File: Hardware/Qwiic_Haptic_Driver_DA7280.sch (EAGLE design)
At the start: 30 parts, among them J1 QWIIC_RIGHT_ANGLE, J2 QWIIC_RIGHT_ANGLE, M1 G1040003D_LRA_CASTELLATED, U1 HAPTIC_DRIVER_DA7280

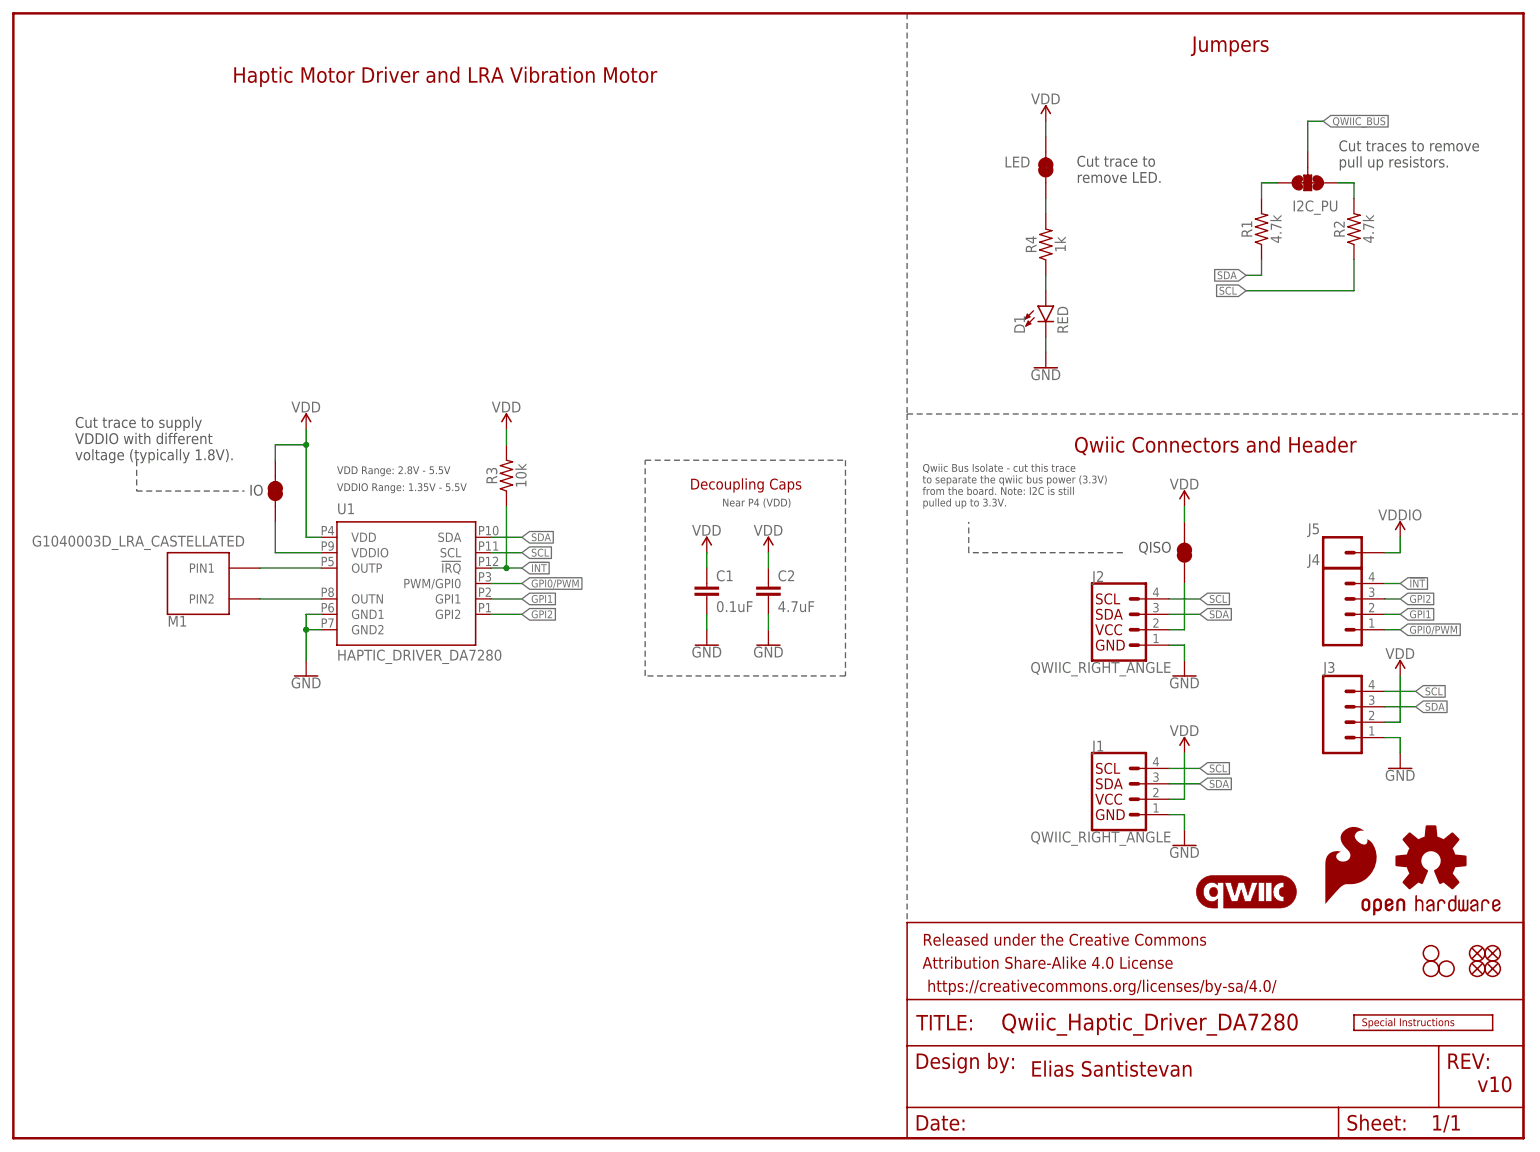
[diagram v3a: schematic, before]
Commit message: Adds second qwiic connecter to "qwiic bus" net so that the respective jumper can disconnect both
* Adds some power symbols
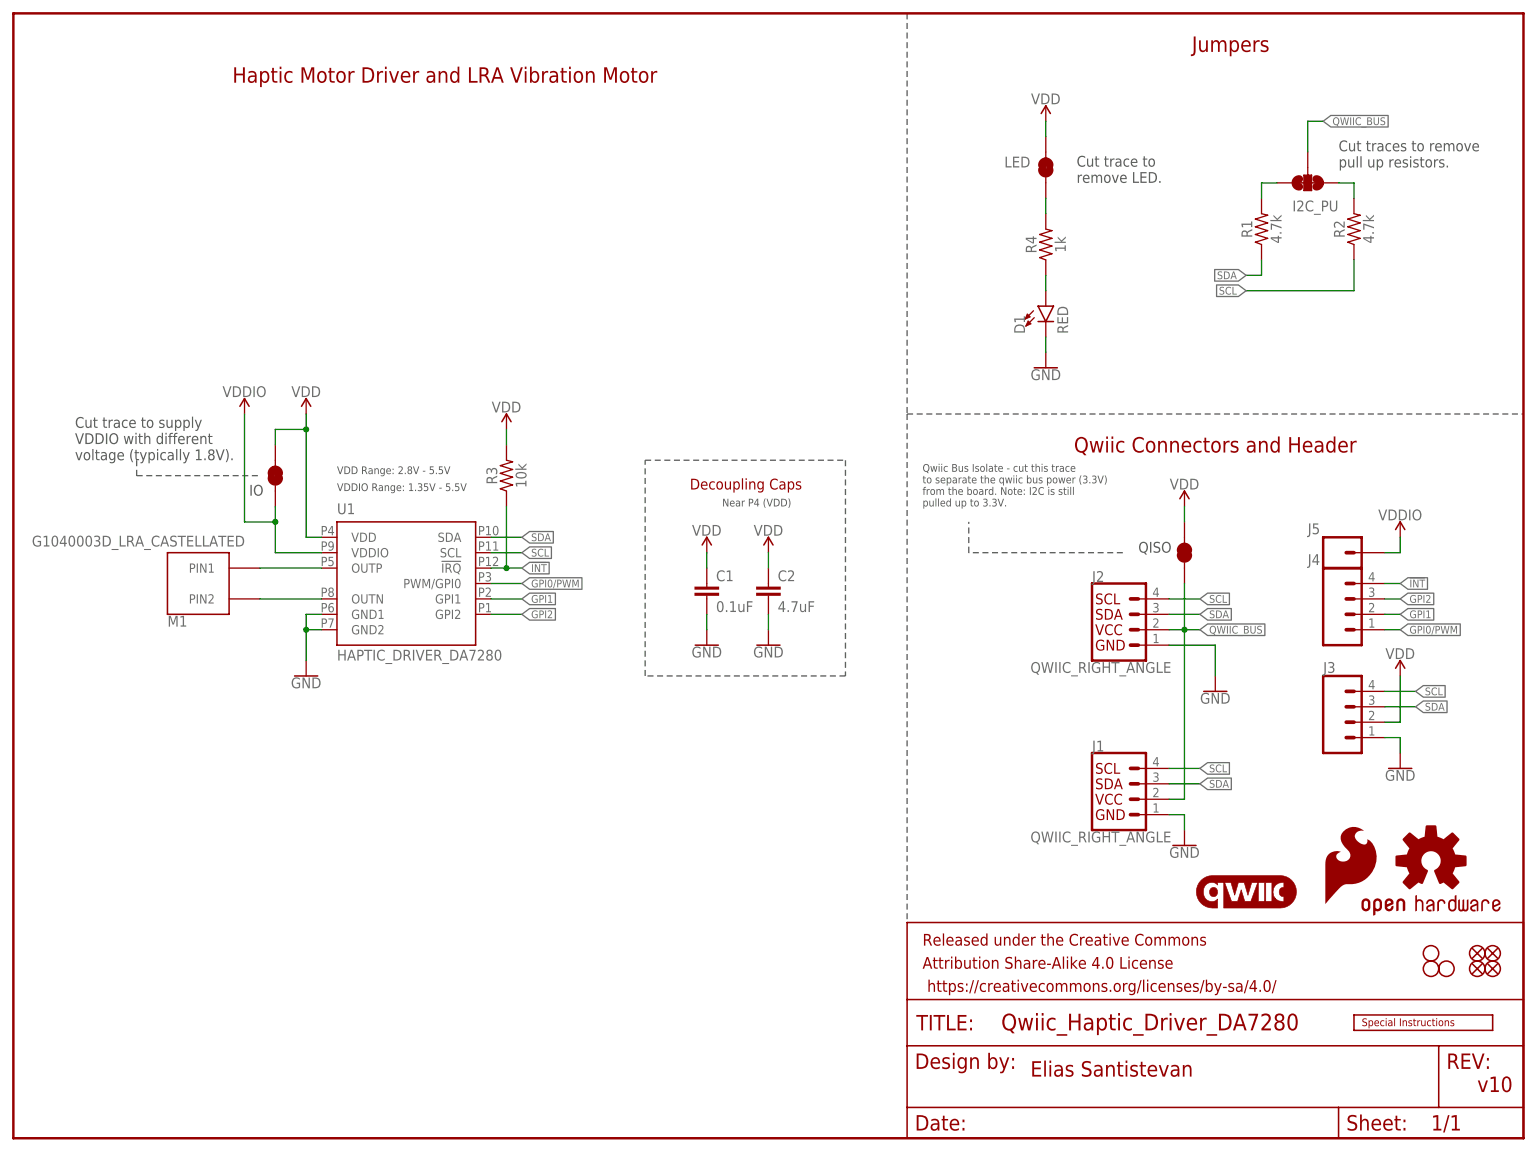
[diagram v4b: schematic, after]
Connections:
- net QWIIC_BUS: now also J1.2
- net VDD: no longer J1.2
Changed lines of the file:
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@@
 <part name="SUPPLY14" library="SparkFun-PowerSymbols" deviceset="VDD" device=""/>
 <part name="SUPPLY1" library="SparkFun-PowerSymbols" deviceset="VDD" device=""/>
-<part name="SUPPLY5" library="SparkFun-PowerSymbols" deviceset="VDD" device=""/>
 <part name="SUPPLY2" library="SparkFun-PowerSymbols" deviceset="VDD" device=""/>
 <part name="J5" library="SparkFun-Connectors" deviceset="CONN_01" device="PTH_NO_SILK_YES_STOP"/>
@@
 <part name="LOGO2" library="SparkFun-Aesthetics" deviceset="OSHW-LOGO" device="S"/>
 <part name="LOGO4" library="SparkFun-Aesthetics" deviceset="SFE_LOGO_FLAME" device=".1_INCH"/>
+<part name="SUPPLY4" library="SparkFun-PowerSymbols" deviceset="VDDIO" device=""/>
 </parts>
 <sheets>
@@
 voltage (typically 1.8V).
 </text>
-<wire x1="20.32" y1="111.76" x2="20.32" y2="106.68" width="0.2032" layer="97" style="dashdot"/>
-<wire x1="20.32" y1="106.68" x2="38.1" y2="106.68" width="0.2032" layer="97" style="dashdot"/>
+<wire x1="20.32" y1="111.76" x2="20.32" y2="109.22" width="0.2032" layer="97" style="dashdot"/>
+<wire x1="20.32" y1="109.22" x2="40.64" y2="109.22" width="0.2032" layer="97" style="dashdot"/>
 <text x="185.42" y="96.52" size="1.778" layer="97" font="vector">QISO</text>
 <text x="149.86" y="104.14" size="1.27" layer="97" font="vector">Qwiic Bus Isolate - cut this trace
@@
 <attribute name="VALUE" x="193.04" y="48.006" size="1.778" layer="96" font="vector" align="top-center"/>
 </instance>
-<instance part="GND3" gate="1" x="193.04" y="76.2" smashed="yes">
-<attribute name="VALUE" x="193.04" y="75.946" size="1.778" layer="96" font="vector" align="top-center"/>
+<instance part="GND3" gate="1" x="198.12" y="73.66" smashed="yes">
+<attribute name="VALUE" x="198.12" y="73.406" size="1.778" layer="96" font="vector" align="top-center"/>
 </instance>
 <instance part="GND4" gate="1" x="228.6" y="60.96" smashed="yes">
@@
 <attribute name="VALUE" x="124.46" y="81.026" size="1.778" layer="96" align="top-center"/>
 </instance>
-<instance part="JP2" gate="G$1" x="43.18" y="106.68" smashed="yes" rot="R90"/>
-<instance part="SUPPLY10" gate="VDD" x="48.26" y="116.84" smashed="yes">
-<attribute name="VALUE" x="48.26" y="119.634" size="1.778" layer="96" align="bottom-center"/>
+<instance part="JP2" gate="G$1" x="43.18" y="109.22" smashed="yes" rot="R90"/>
+<instance part="SUPPLY10" gate="VDD" x="48.26" y="119.38" smashed="yes">
+<attribute name="VALUE" x="48.26" y="122.174" size="1.778" layer="96" align="bottom-center"/>
 </instance>
 <instance part="SUPPLY11" gate="VDD" x="81.28" y="116.84" smashed="yes">
@@
 <instance part="SUPPLY1" gate="VDD" x="193.04" y="104.14" smashed="yes">
 <attribute name="VALUE" x="193.04" y="106.934" size="1.778" layer="96" align="bottom-center"/>
-</instance>
-<instance part="SUPPLY5" gate="VDD" x="193.04" y="63.5" smashed="yes">
-<attribute name="VALUE" x="193.04" y="66.294" size="1.778" layer="96" align="bottom-center"/>
 </instance>
 <instance part="SUPPLY2" gate="VDD" x="228.6" y="76.2" smashed="yes">
@@
 <instance part="LOGO2" gate="G$1" x="233.68" y="45.72" smashed="yes"/>
 <instance part="LOGO4" gate="G$1" x="215.9" y="38.1" smashed="yes"/>
+<instance part="SUPPLY4" gate="G$1" x="38.1" y="119.38" smashed="yes">
+<attribute name="VALUE" x="38.1" y="122.174" size="1.778" layer="96" align="bottom-center"/>
+</instance>
 </instances>
 <busses>
@@
 <pinref part="J2" gate="G$1" pin="1"/>
 <pinref part="GND3" gate="1" pin="GND"/>
-<wire x1="190.5" y1="81.28" x2="193.04" y2="81.28" width="0.1524" layer="91"/>
-<wire x1="193.04" y1="81.28" x2="193.04" y2="78.74" width="0.1524" layer="91"/>
+<wire x1="190.5" y1="81.28" x2="198.12" y2="81.28" width="0.1524" layer="91"/>
+<wire x1="198.12" y1="81.28" x2="198.12" y2="76.2" width="0.1524" layer="91"/>
 </segment>
 <segment>
@@
 <pinref part="U1" gate="G$1" pin="VDD"/>
 <wire x1="50.8" y1="99.06" x2="48.26" y2="99.06" width="0.1524" layer="91"/>
-<wire x1="48.26" y1="99.06" x2="48.26" y2="114.3" width="0.1524" layer="91"/>
+<wire x1="48.26" y1="99.06" x2="48.26" y2="116.84" width="0.1524" layer="91"/>
 <pinref part="JP2" gate="G$1" pin="2"/>
-<wire x1="43.18" y1="111.76" x2="43.18" y2="114.3" width="0.1524" layer="91"/>
-<wire x1="43.18" y1="114.3" x2="48.26" y2="114.3" width="0.1524" layer="91"/>
-<junction x="48.26" y="114.3"/>
+<wire x1="43.18" y1="114.3" x2="43.18" y2="116.84" width="0.1524" layer="91"/>
+<wire x1="43.18" y1="116.84" x2="48.26" y2="116.84" width="0.1524" layer="91"/>
+<junction x="48.26" y="116.84"/>
 <pinref part="SUPPLY10" gate="VDD" pin="VDD"/>
-<wire x1="48.26" y1="114.3" x2="48.26" y2="116.84" width="0.1524" layer="91"/>
+<wire x1="48.26" y1="116.84" x2="48.26" y2="119.38" width="0.1524" layer="91"/>
 </segment>
 <segment>
@@
 <pinref part="SUPPLY14" gate="VDD" pin="VDD"/>
 <wire x1="170.18" y1="165.1" x2="170.18" y2="167.64" width="0.1524" layer="91"/>
-</segment>
-<segment>
-<pinref part="J1" gate="G$1" pin="2"/>
-<wire x1="190.5" y1="55.88" x2="193.04" y2="55.88" width="0.1524" layer="91"/>
-<wire x1="193.04" y1="55.88" x2="193.04" y2="63.5" width="0.1524" layer="91"/>
-<pinref part="SUPPLY5" gate="VDD" pin="VDD"/>
 </segment>
 <segment>
@@
 <pinref part="JP2" gate="G$1" pin="1"/>
 <wire x1="43.18" y1="96.52" x2="43.18" y2="101.6" width="0.1524" layer="91"/>
+<pinref part="SUPPLY4" gate="G$1" pin="VDDIO"/>
+<wire x1="43.18" y1="101.6" x2="43.18" y2="104.14" width="0.1524" layer="91"/>
+<wire x1="43.18" y1="101.6" x2="38.1" y2="101.6" width="0.1524" layer="91"/>
+<wire x1="38.1" y1="101.6" x2="38.1" y2="119.38" width="0.1524" layer="91"/>
+<junction x="43.18" y="101.6"/>
 </segment>
 <segment>
@@
 <wire x1="193.04" y1="83.82" x2="193.04" y2="91.44" width="0.1524" layer="91"/>
 <pinref part="JP4" gate="G$1" pin="1"/>
-</segment>
-<segment>
+<pinref part="J1" gate="G$1" pin="2"/>
+<wire x1="190.5" y1="55.88" x2="193.04" y2="55.88" width="0.1524" layer="91"/>
+<wire x1="193.04" y1="83.82" x2="193.04" y2="55.88" width="0.1524" layer="91"/>
+<junction x="193.04" y="83.82"/>
+<wire x1="193.04" y1="83.82" x2="195.58" y2="83.82" width="0.1524" layer="91"/>
+<label x="195.58" y="83.82" size="1.27" layer="95" xref="yes"/>
+</segment>
+<segment>
